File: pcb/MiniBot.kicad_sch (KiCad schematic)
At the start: 27 parts, among them IC1 MIC23050-SYML-TR, IC2 RT9527GQW, J1 GSB1C41110SSHR, J4 Conn_01x02, J5 Conn_01x02, J6 Conn_01x01, J7 Conn_01x01, U1 ESP32-C3-MINI-1-H4X

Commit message: big updates
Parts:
- removed D4: LED_Dual_KAKA, SamacSys_Parts:SB0603WC01-RG, symbol Device:LED_Dual_KAKA
- removed IC2: RT9527GQW, SON50P200X200X80-9N, symbol SamacSys_Parts:RT9527GQW
- removed J6, J7: Conn_01x01, TestPoint:TestPoint_Pad_D1.0mm, symbol Connector_Generic:Conn_01x01
- removed R16: 300, Resistor_SMD:R_0402_1005Metric, symbol Device:R
- added C14, C15, C17, C18, C20: 0.1uF, Capacitor_SMD:C_0402_1005Metric, symbol Device:C
- added C16, C19: 4.7uF, Capacitor_SMD:C_0402_1005Metric, symbol Device:C
- added D2, D3: LED, Diode_SMD:D_0402_1005Metric, symbol Device:LED
- added R21, R22, R25: 10k, Resistor_SMD:R_0402_1005Metric, symbol Device:R
- added S3: SSU-121BRT, SSU121BRT, symbol SamacSys_Parts:SSU-121BRT
- added U2: MCP73832-2-OT, Package_TO_SOT_SMD:SOT-23-5, symbol Battery_Management:MCP73832-2-OT
- C11: value 500nF -> 4.7uF
- C12: value 0.1uF -> 1uF
- R14: value 4k -> 261
- R15: value 300 -> 1k
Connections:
- net IO1 is gone; now on net M1_IN2: U1.16 (IO10)
- net +3V3: now also R14.1, C14.1, C19.2, C20.1, R21.1, R22.1
- net +5V: now also C17.1, D2.2 (A), U2.4 (V_{DD}); no longer R15.1
- net AMP: now also U1.12 (IO0); no longer U1.5 (IO2)
- net GND: now also C11.1, C14.2, C15.2, C16.2, C17.2, C18.2, C19.1, C20.2, D3.1 (K), R25.2, U2.2 (V_{SS}); no longer C11.2, R14.2
- net M0_IN1: now also U1.20 (IO6); no longer U1.21 (IO7)
- net M0_IN2: now also U1.19 (IO5); no longer U1.22 (IO8)
- net M1_IN1: now also U1.18 (IO4); no longer U1.19 (IO5)
- net M1_IN2: no longer U1.20 (IO6)
- net M_SLEEP: now also U1.21 (IO7); no longer U1.18 (IO4)
- net VDC: now also C16.1, S3.C1 (NO); no longer C8.1, J5.2 (Pin_2)
- net VSENSE: now also C15.1
- net at R15.2: now also U2.1 (STAT)
- net IO0: no longer names the net of U1.6 (IO3)
- new net: D2.1 (K), R15.1
- new net: D3.2 (A), R14.2
- new net: R25.1, U2.5 (PROG)
- new net +BATT: C11.2, C18.1, C8.1, J5.2 (Pin_2), S3.B1 (COM), U2.3 (V_{BAT})
- new net GPIO2: R22.2, U1.5 (IO2)
- new net GPIO8: R21.2, U1.22 (IO8)
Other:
- moved on the sheet: C10, C8, C9, IC1, J5, L1, R17, R18

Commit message: complete overhaul wip
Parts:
- removed J4: Conn_01x02, SamacSys_Parts:Transducer, symbol Connector_Generic:Conn_01x02
- added C22: 0.1uF, Capacitor_SMD:C_0402_1005Metric, symbol Device:C
- added J1: Conn_01x08, Connector_JST:JST_SH_BM08B-SRSS-TB_1x08-1MP_P1.00mm_Vertical, symbol Connector_Generic:Conn_01x08
- added R24: 390k, Resistor_SMD:R_0402_1005Metric, symbol Device:R
- added R25: 15k, Resistor_SMD:R_0402_1005Metric, symbol Device:R
- added U2: TLV493D, Package_TO_SOT_SMD:SOT-23-6, symbol Sensor_Magnetic:TLV493D
- J2: renamed from J5; footprint Connector_JST:JST_PH_S2B-PH-K_1x02_P2.00mm_Horizontal -> Connector_JST:JST_PH_B2B-PH-K_1x02_P2.00mm_Vertical
- renumbered C19 to C1, C11 to C10, C9 to C11, C18 to C12, C14 to C13, C20 to C2, C12 to C3, C13 to C4, C15 to C5, C10 to C6, C16 to C7, C17 to C8, C8 to C9, D3 to D1, J1 to J3, R19 to R1, R12 to R10, R13 to R11, R14 to R2, R21 to R3, R22 to R4, R20 to R5, R17 to R6, R18 to R7, R25 to R8, R15 to R9, S3 to S1, S1 to S2, S2 to S3, U2 to U3
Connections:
- net +3V3: now also U2.4 (VDD)
- net +5V: now also S1.A2; no longer D2.2 (A)
- net +BATT: now also D2.2 (A), S1.B2; no longer S1.B1 (COM)
- net GND: now also C22.2, R25.2, U2.2 (GND), U2.3 (GND), U2.5 (GND)
- net VDC: now also R24.1
- net SDA: now reaches U1.30 (RXD0)
- net SDA: now also U2.6 (SDA/ADDR)
- net SCL: now reaches U1.31 (TXD0)
- net SCL: now also U2.1 (SCL/INT)
- net AMP: no longer names the net of U1.12 (IO0)
- net M0_IN1: no longer names the net of U1.20 (IO6)
- net M0_IN2: no longer names the net of U1.19 (IO5)
- net M1_IN1: no longer names the net of U1.18 (IO4)
- net M1_IN2: no longer names the net of U1.16 (IO10)
- net M_SLEEP: no longer names the net of U1.21 (IO7)
- new net M0_A1: J1.1 (Pin_1)
- new net M0_A2: J1.2 (Pin_2)
- new net M0_B1: J1.7 (Pin_7)
- new net M0_B2: J1.8 (Pin_8)
- new net M1_A1: J1.3 (Pin_3)
- new net M1_A2: J1.4 (Pin_4)
- new net M1_B1: J1.5 (Pin_5)
- new net M1_B2: J1.6 (Pin_6)
- new net VREF: C22.1, R24.2, R25.1
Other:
- removed sheet Ultrasonic Amplifier
- sheet MotorDriver0 ports: added DIR, EN, MOTA1, MOTA2, MOTB1, MOTB2, RST, STEP, VREF; removed IN1, IN2, SLEEP
- sheet MotorDriver1 ports: added DIR, EN, MOTA1, MOTA2, MOTB1, MOTB2, RST, STEP, VREF; removed IN1, IN2, SLEEP
- moved on the sheet: C1, C2, U1

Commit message: lots of pcb work, test code, and final fw framework starting
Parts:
- removed C10, C11: 4.7uF, Capacitor_SMD:C_0402_1005Metric, symbol Device:C
- removed C12, C13: 0.1uF, Capacitor_SMD:C_0402_1005Metric, symbol Device:C
- removed S1: SSU-121BRT, SSU121BRT, symbol SamacSys_Parts:SSU-121BRT
- removed U2: TLV493D, Package_TO_SOT_SMD:SOT-23-6, symbol Sensor_Magnetic:TLV493D
- added C23: 0.1uF, Capacitor_SMD:C_0402_1005Metric, symbol Device:C
- added IC1: MMC5633NJL, BGA4C40P2X2_85X85X60, symbol SamacSys_Parts:MMC5633NJL
- added R1, R2: 5.1k, Resistor_SMD:R_0402_1005Metric, symbol Device:R
- added S1: PCM12SMTR, PCM12SMTR, symbol SamacSys_Parts:PCM12SMTR
- J2: footprint Connector_JST:JST_PH_B2B-PH-K_1x02_P2.00mm_Vertical -> Connector_JST:JST_PH_S2B-PH-K_1x02_P2.00mm_Horizontal
- renumbered C9 to C10, C22 to C4, C4 to C5, C5 to C6, C6 to C7, C7 to C8, C8 to C9, IC1 to IC2, R6 to R10, R7 to R11, R8 to R12, R9 to R13, R10 to R14, R11 to R15, R1 to R3, R2 to R4, R3 to R5, R4 to R6, R24 to R7, R25 to R8, R5 to R9
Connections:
- net +3V3: now also IC1.B1 (VDD), R1.1, R2.1
- net +5V: now also S1.1 (NC)
- net +BATT: now also S1.3 (NO)
- net GND: now also C23.2, IC1.A1 (VSA)
- net SCL: now also IC1.A2 (SCL), R1.2
- net SDA: now also IC1.B2 (SDA), R2.2
- net VDC: now also C23.1, S1.2 (COM)
- net M0_STEP: now reaches U1.16 (IO10)
- net M0_DIR: now reaches U1.18 (IO4)
- net M1_STEP: now reaches U1.19 (IO5)
- net M1_DIR: now reaches U1.20 (IO6)
- net M_EN: now reaches U1.21 (IO7)
- net M_RST: now reaches U1.6 (IO3)
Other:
- moved on the sheet: C1, C10, C2, C9, D2, R12, R13, U3

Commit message: refining pcb and simulator code
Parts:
- removed R4: 261, Resistor_SMD:R_0402_1005Metric, symbol Device:R
- added R17: 1k, Resistor_SMD:R_0402_1005Metric, symbol Device:R
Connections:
- net +3V3: now also R17.1
- net at D1.2 (A): now also R17.2
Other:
- moved on the sheet: C1, C2, IC1, R1, R2

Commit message: getting close to order state
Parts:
- added J4: Conn_01x01, TestPoint:TestPoint_Pad_D1.0mm, symbol Connector_Generic:Conn_01x01
- added JP1, JP2: Jumper_3_Bridged12, Jumper:SolderJumper-3_P1.3mm_Bridged12_RoundedPad1.0x1.5mm, symbol Jumper:Jumper_3_Bridged12
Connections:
- net +3V3: now also R7.1, JP1.1 (A), JP2.3 (B)
- net GND: now also JP1.3 (B), JP2.1 (A)
- net VDC: no longer R7.1
- net GPIO0: now reaches U1.12 (IO0)
- net GPIO0: now also J4.1 (Pin_1)
- new net MODE1: JP2.2 (C)
- new net MODE2: JP1.2 (C)
- no-connect marks 0 -> 24
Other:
- sheet MotorDriver0 ports: added MODE1, MODE2; removed none
- sheet MotorDriver1 ports: added MODE1, MODE2; removed none
- moved on the sheet: C1, C10, C2, C23, C3, C4, C5, C6, C7, C8, C9, D1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

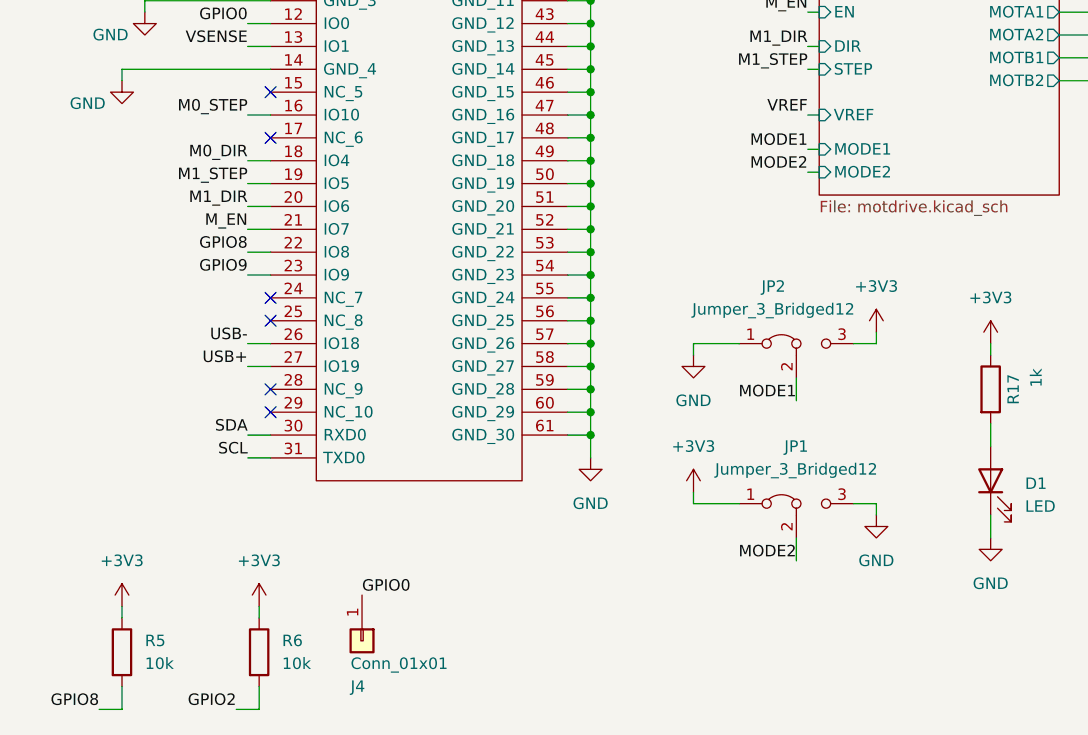
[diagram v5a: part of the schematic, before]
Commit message: reorg and write device ID to NVS
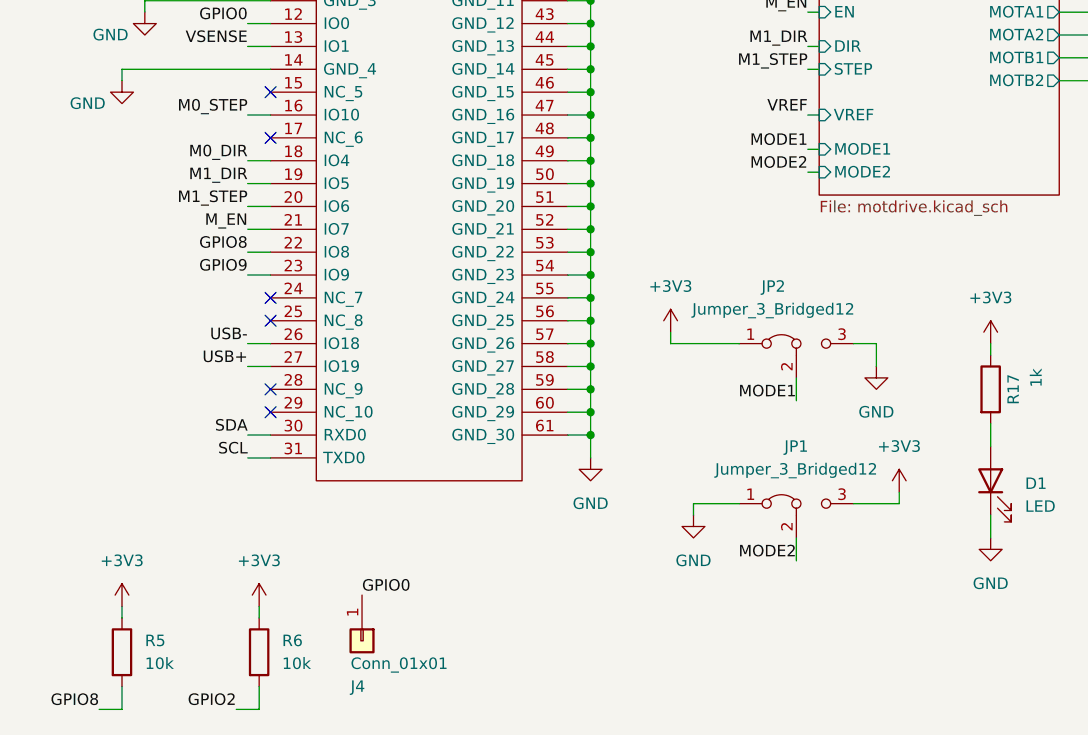
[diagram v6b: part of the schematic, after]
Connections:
- net +3V3: now also JP1.3 (B), JP2.1 (A); no longer JP1.1 (A), JP2.3 (B)
- net GND: now also JP1.1 (A), JP2.3 (B); no longer JP1.3 (B), JP2.1 (A)
- net M1_DIR: now also U1.19 (IO5); no longer U1.20 (IO6)
- net M1_STEP: now also U1.20 (IO6); no longer U1.19 (IO5)
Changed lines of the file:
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@@
     (stroke (width 0) (type default))
   )
-  (wire (pts (xy 107.95 96.52) (xy 102.87 96.52))
+  (wire (pts (xy 107.95 96.52) (xy 100.33 96.52))
     (stroke (width 0) (type default))
   )
@@
     (stroke (width 0) (type default))
   )
-  (wire (pts (xy 102.87 96.52) (xy 102.87 97.79))
-    (stroke (width 0) (type default))
-  )
   (wire (pts (xy 271.78 59.69) (xy 274.32 59.69))
     (stroke (width 0) (type default))
@@
     (stroke (width 0) (type default))
   )
+  (wire (pts (xy 102.87 114.3) (xy 102.87 115.57))
+    (stroke (width 0) (type default))
+  )
   (wire (pts (xy 91.44 106.68) (xy 91.44 109.22))
     (stroke (width 0) (type default))
   )
+  (wire (pts (xy 123.19 96.52) (xy 123.19 99.06))
+    (stroke (width 0) (type default))
+  )
   (wire (pts (xy 88.9 60.96) (xy 91.44 60.96))
     (stroke (width 0) (type default))
@@
     (stroke (width 0) (type default))
   )
-  (wire (pts (xy 123.19 114.3) (xy 123.19 115.57))
-    (stroke (width 0) (type default))
-  )
   (wire (pts (xy 91.44 93.98) (xy 91.44 96.52))
     (stroke (width 0) (type default))
@@
     (stroke (width 0) (type default))
   )
-  (wire (pts (xy 102.87 114.3) (xy 102.87 113.03))
-    (stroke (width 0) (type default))
-  )
-  (wire (pts (xy 123.19 95.25) (xy 123.19 96.52))
-    (stroke (width 0) (type default))
-  )
   (wire (pts (xy 250.19 30.48) (xy 251.46 30.48))
     (stroke (width 0) (type default))
@@
     (stroke (width 0) (type default))
   )
-  (wire (pts (xy 120.65 114.3) (xy 123.19 114.3))
+  (wire (pts (xy 120.65 114.3) (xy 125.73 114.3))
     (stroke (width 0) (type default))
   )
@@
     (stroke (width 0) (type default))
   )
+  (wire (pts (xy 125.73 113.03) (xy 125.73 114.3))
+    (stroke (width 0) (type default))
+  )
   (wire (pts (xy 54.61 33.02) (xy 48.26 33.02))
     (stroke (width 0) (type default))
@@
   )
   (wire (pts (xy 48.26 33.02) (xy 48.26 36.83))
+    (stroke (width 0) (type default))
+  )
+  (wire (pts (xy 100.33 95.25) (xy 100.33 96.52))
     (stroke (width 0) (type default))
   )
@@
     (effects (font (size 1.27 1.27)) (justify right bottom))
   )
-  (label "M1_STEP" (at 53.34 78.74 180) (fields_autoplaced)
+  (label "M1_DIR" (at 53.34 78.74 180) (fields_autoplaced)
     (effects (font (size 1.27 1.27)) (justify right bottom))
   )
@@
   )
   (label "M0_DIR" (at 53.34 76.2 180) (fields_autoplaced)
-    (effects (font (size 1.27 1.27)) (justify right bottom))
-  )
-  (label "M1_DIR" (at 53.34 81.28 180) (fields_autoplaced)
     (effects (font (size 1.27 1.27)) (justify right bottom))
   )
@@
   )
   (label "CFF" (at 204.47 41.91 180) (fields_autoplaced)
+    (effects (font (size 1.27 1.27)) (justify right bottom))
+  )
+  (label "M1_STEP" (at 53.34 81.28 180) (fields_autoplaced)
     (effects (font (size 1.27 1.27)) (justify right bottom))
   )
@@
     )
   )
+  (symbol (lib_id "power:GND") (at 123.19 99.06 0) (unit 1)
+    (in_bom yes) (on_board yes) (dnp no) (fields_autoplaced)
+    (property "Reference" "#PWR038" (at 123.19 105.41 0)
+      (effects (font (size 1.27 1.27)) hide)
+    )
+    (property "Value" "GND" (at 123.19 104.14 0)
+      (effects (font (size 1.27 1.27)))
+    )
+    (property "Footprint" "" (at 123.19 99.06 0)
+      (effects (font (size 1.27 1.27)) hide)
+    )
+    (property "Datasheet" "" (at 123.19 99.06 0)
+      (effects (font (size 1.27 1.27)) hide)
+    )
+    (pin "1")
+    (instances
+      (project "MiniBot"
+        (path "/0e598331-3211-4e8a-a305-31a83585854d"
+          (reference "#PWR038") (unit 1)
+        )
+      )
+    )
+  )
   (symbol (lib_id "power:VDC") (at 245.11 62.23 90) (unit 1)
     (in_bom yes) (on_board yes) (dnp no) (fields_autoplaced)
@@
     )
   )
-  (symbol (lib_id "power:+3V3") (at 123.19 95.25 0) (unit 1)
-    (in_bom yes) (on_board yes) (dnp no) (fields_autoplaced)
-    (property "Reference" "#PWR056" (at 123.19 99.06 0)
-      (effects (font (size 1.27 1.27)) hide)
-    )
-    (property "Value" "+3V3" (at 123.19 90.17 0)
-      (effects (font (size 1.27 1.27)))
-    )
-    (property "Footprint" "" (at 123.19 95.25 0)
-      (effects (font (size 1.27 1.27)) hide)
-    )
-    (property "Datasheet" "" (at 123.19 95.25 0)
-      (effects (font (size 1.27 1.27)) hide)
-    )
-    (pin "1")
-    (instances
-      (project "MiniBot"
-        (path "/0e598331-3211-4e8a-a305-31a83585854d"
-          (reference "#PWR056") (unit 1)
-        )
-      )
-    )
-  )
   (symbol (lib_id "power:+3V3") (at 54.61 180.34 0) (unit 1)
     (in_bom yes) (on_board yes) (dnp no) (fields_autoplaced)
@@
         (path "/0e598331-3211-4e8a-a305-31a83585854d"
           (reference "D1") (unit 1)
+        )
+      )
+    )
+  )
+  (symbol (lib_id "power:GND") (at 102.87 115.57 0) (unit 1)
+    (in_bom yes) (on_board yes) (dnp no) (fields_autoplaced)
+    (property "Reference" "#PWR057" (at 102.87 121.92 0)
+      (effects (font (size 1.27 1.27)) hide)
+    )
+    (property "Value" "GND" (at 102.87 120.65 0)
+      (effects (font (size 1.27 1.27)))
+    )
+    (property "Footprint" "" (at 102.87 115.57 0)
+      (effects (font (size 1.27 1.27)) hide)
+    )
+    (property "Datasheet" "" (at 102.87 115.57 0)
+      (effects (font (size 1.27 1.27)) hide)
+    )
+    (pin "1")
+    (instances
+      (project "MiniBot"
+        (path "/0e598331-3211-4e8a-a305-31a83585854d"
+          (reference "#PWR057") (unit 1)
         )
       )
@@
     )
   )
+  (symbol (lib_id "power:+3V3") (at 125.73 113.03 0) (unit 1)
+    (in_bom yes) (on_board yes) (dnp no) (fields_autoplaced)
+    (property "Reference" "#PWR067" (at 125.73 116.84 0)
+      (effects (font (size 1.27 1.27)) hide)
+    )
+    (property "Value" "+3V3" (at 125.73 107.95 0)
+      (effects (font (size 1.27 1.27)))
+    )
+    (property "Footprint" "" (at 125.73 113.03 0)
+      (effects (font (size 1.27 1.27)) hide)
+    )
+    (property "Datasheet" "" (at 125.73 113.03 0)
+      (effects (font (size 1.27 1.27)) hide)
+    )
+    (pin "1")
+    (instances
+      (project "MiniBot"
+        (path "/0e598331-3211-4e8a-a305-31a83585854d"
+          (reference "#PWR067") (unit 1)
+        )
+      )
+    )
+  )
   (symbol (lib_id "power:GND") (at 91.44 109.22 0) (unit 1)
     (in_bom yes) (on_board yes) (dnp no) (fields_autoplaced)
@@
         (path "/0e598331-3211-4e8a-a305-31a83585854d"
           (reference "#PWR018") (unit 1)
-        )
-      )
-    )
-  )
-  (symbol (lib_id "power:GND") (at 123.19 115.57 0) (unit 1)
-    (in_bom yes) (on_board yes) (dnp no) (fields_autoplaced)
-    (property "Reference" "#PWR047" (at 123.19 121.92 0)
-      (effects (font (size 1.27 1.27)) hide)
-    )
-    (property "Value" "GND" (at 123.19 120.65 0)
-      (effects (font (size 1.27 1.27)))
-    )
-    (property "Footprint" "" (at 123.19 115.57 0)
-      (effects (font (size 1.27 1.27)) hide)
-    )
-    (property "Datasheet" "" (at 123.19 115.57 0)
-      (effects (font (size 1.27 1.27)) hide)
-    )
-    (pin "1")
-    (instances
-      (project "MiniBot"
-        (path "/0e598331-3211-4e8a-a305-31a83585854d"
-          (reference "#PWR047") (unit 1)
         )
       )
@@
     )
   )
-  (symbol (lib_id "power:+3V3") (at 102.87 113.03 0) (unit 1)
-    (in_bom yes) (on_board yes) (dnp no) (fields_autoplaced)
-    (property "Reference" "#PWR050" (at 102.87 116.84 0)
-      (effects (font (size 1.27 1.27)) hide)
-    )
-    (property "Value" "+3V3" (at 102.87 107.95 0)
-      (effects (font (size 1.27 1.27)))
-    )
-    (property "Footprint" "" (at 102.87 113.03 0)
-      (effects (font (size 1.27 1.27)) hide)
-    )
-    (property "Datasheet" "" (at 102.87 113.03 0)
-      (effects (font (size 1.27 1.27)) hide)
-    )
-    (pin "1")
-    (instances
-      (project "MiniBot"
-        (path "/0e598331-3211-4e8a-a305-31a83585854d"
-          (reference "#PWR050") (unit 1)
-        )
-      )
-    )
-  )
   (symbol (lib_id "power:GND") (at 156.21 119.38 0) (unit 1)
     (in_bom yes) (on_board yes) (dnp no) (fields_autoplaced)
@@
         (path "/0e598331-3211-4e8a-a305-31a83585854d"
           (reference "#PWR042") (unit 1)
-        )
-      )
-    )
-  )
-  (symbol (lib_id "power:GND") (at 102.87 97.79 0) (unit 1)
-    (in_bom yes) (on_board yes) (dnp no) (fields_autoplaced)
-    (property "Reference" "#PWR045" (at 102.87 104.14 0)
-      (effects (font (size 1.27 1.27)) hide)
-    )
-    (property "Value" "GND" (at 102.87 102.87 0)
-      (effects (font (size 1.27 1.27)))
-    )
-    (property "Footprint" "" (at 102.87 97.79 0)
-      (effects (font (size 1.27 1.27)) hide)
-    )
-    (property "Datasheet" "" (at 102.87 97.79 0)
-      (effects (font (size 1.27 1.27)) hide)
-    )
-    (pin "1")
-    (instances
-      (project "MiniBot"
-        (path "/0e598331-3211-4e8a-a305-31a83585854d"
-          (reference "#PWR045") (unit 1)
         )
       )
@@
         )
       )
+    )
+  )
+  (symbol (lib_id "power:+3V3") (at 100.33 95.25 0) (unit 1)
+    (in_bom yes) (on_board yes) (dnp no) (fields_autoplaced)
+    (property "Reference" "#PWR037" (at 100.33 99.06 0)
+      (effects (font (size 1.27 1.27)) hide)
+    )
+    (property "Value" "+3V3" (at 100.33 90.17 0)
+      (effects (font (size 1.27 1.27)))
+    )
+    (property "Footprint" "" (at 100.33 95.25 0)
+      (effects (font (size 1.27 1.27)) hide)
+    )
+    (property "Datasheet" "" (at 100.33 95.25 0)
+      (effects (font (size 1.27 1.27)) hide)
+    )
+    (pin "1")
+    (instances
+      (project "MiniBot"
+        (path "/0e598331-3211-4e8a-a305-31a83585854d"
+          (reference "#PWR037") (unit 1)
+        )
+      )
